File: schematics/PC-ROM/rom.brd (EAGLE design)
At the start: 40.1 x 49.6 mm, 23 parts

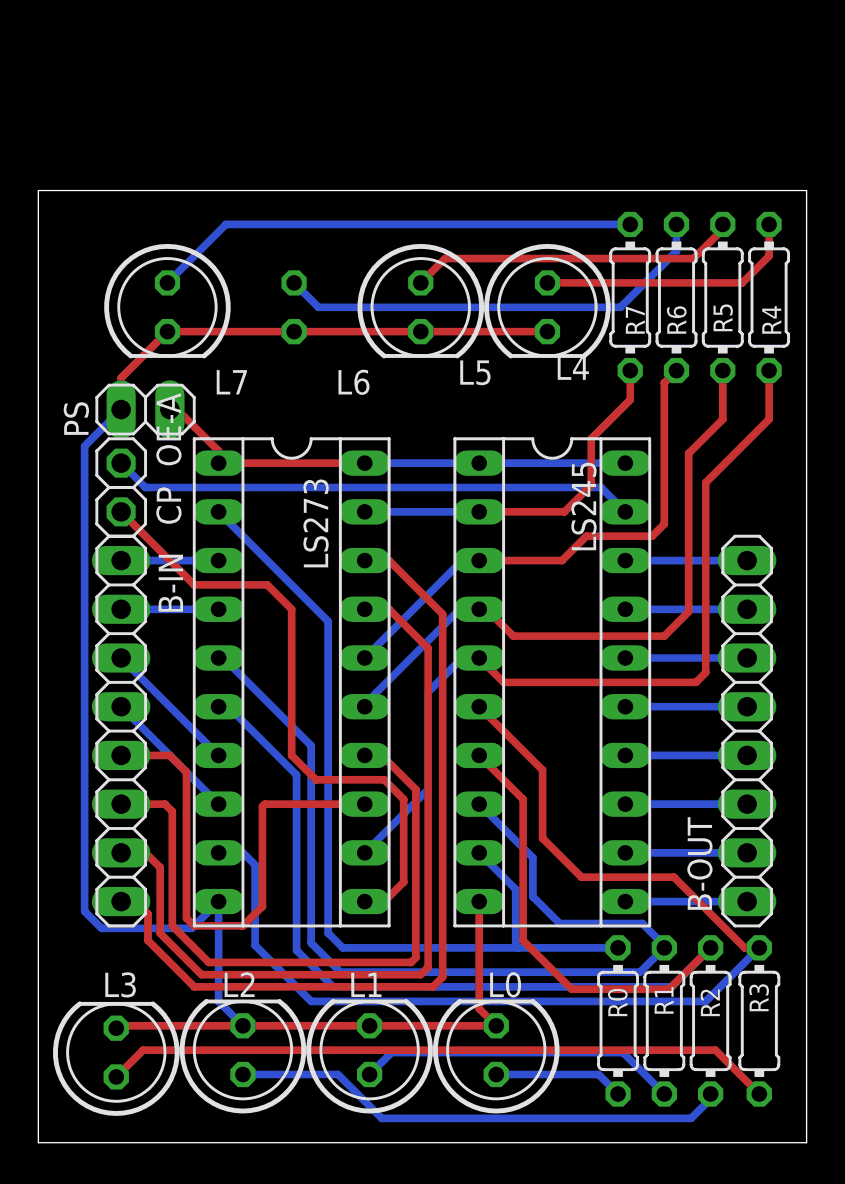
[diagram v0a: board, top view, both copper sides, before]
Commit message: Added sch, brd and gerber file for register, register bus, pc and ROM.
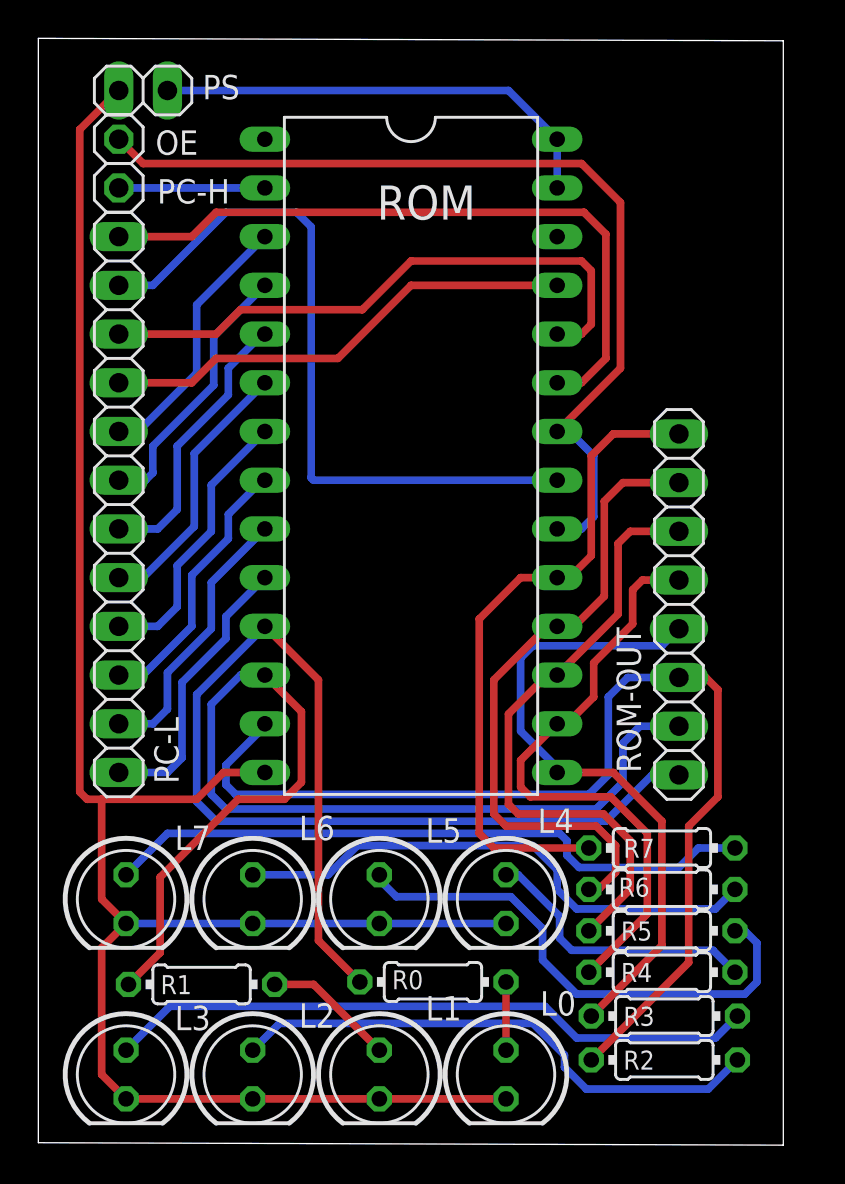
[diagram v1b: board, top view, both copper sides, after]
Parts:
- removed B-IN, B-OUT: (no value), pinhead:1X08
- removed CP, OE-A: (no value), pinhead:1X01
- removed LS245, LS273: (no value), ic-package:SOCKET-20
- added OE, PC-H: (no value), pinhead:1X01
- added PC-L: (no value), pinhead:1X12
- added ROM: (no value), ic-package:DIL28-6
- added ROM-OUT: (no value), pinhead:1X08
- moved R4 35.6 mm to (32.5, 8.89), turned to 180 degrees
- moved R5 33.2 mm to (32.5, 11.0), turned to 180 degrees
- moved L4 30.9 mm to (24.4, 12.7)
- moved L5 30.9 mm to (17.8, 12.7)
- moved L6 30.9 mm to (11.2, 12.7), flipped to the top
- moved L7 30.9 mm to (4.57, 12.7)
- moved R6 30.9 mm to (32.5, 13.2), turned to 180 degrees
- moved R7 28.7 mm to (32.5, 15.4), turned to 180 degrees
- moved R1 24.2 mm to (8.51, 8.26), turned to 180 degrees
- moved PS 16.6 mm to (5.46, 54.9)
- moved R0 9.86 mm to (20.6, 8.38), turned to 180 degrees
- moved R3 4.96 mm to (32.6, 6.60), turned to 180 degrees
- moved R2 3.15 mm to (32.6, 4.32), turned to 180 degrees
- moved L1 1.37 mm to (17.8, 3.56), turned to 270 degrees
- moved L2 1.37 mm to (11.2, 3.56), turned to 270 degrees
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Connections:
- removed net BO0: B-OUT.8, LS245.11
- removed net BO1: B-OUT.7, LS245.12
- removed net BO2: B-OUT.6, LS245.13
- removed net BO3: B-OUT.5, LS245.14
- removed net BO4: B-OUT.4, LS245.15
- removed net BO5: B-OUT.3, LS245.16
- removed net BO6: B-OUT.2, LS245.17
- removed net BO7: B-OUT.1, LS245.18
- removed net CP: CP.1, LS273.11
- removed net D0: B-IN.1, LS273.3
- removed net D1: B-IN.2, LS273.4
- removed net D2: B-IN.3, LS273.7
- removed net D3: B-IN.4, LS273.8
- removed net D4: B-IN.5, LS273.13
- removed net D5: B-IN.6, LS273.14
- removed net D6: B-IN.7, LS273.17
- removed net D7: B-IN.8, LS273.18
- removed net N$18: LS245.19, OE-A.1
- removed net Q0: LS245.9, LS273.2, R0.2
- removed net Q1: LS245.8, LS273.5, R1.2
- removed net Q2: LS245.7, LS273.6, R2.2
- removed net Q3: LS245.6, LS273.9, R3.2
- removed net Q4: LS245.5, LS273.12, R4.2
- removed net Q5: LS245.4, LS273.15, R5.2
- removed net Q6: LS245.3, LS273.16, R6.2
- removed net Q7: LS245.2, LS273.19, R7.2
- new net OE: OE.1, ROM.20, ROM.22
- new net PC0: PC-L.12, ROM.10
- new net PC1: PC-L.11, ROM.9
- new net PC10: PC-L.2, ROM.21
- new net PC11: PC-L.1, ROM.23
- new net PC12: PC-H.1, ROM.2
- new net PC2: PC-L.10, ROM.8
- new net PC3: PC-L.9, ROM.7
- new net PC4: PC-L.8, ROM.6
- new net PC5: PC-L.7, ROM.5
- new net PC6: PC-L.6, ROM.4
- new net PC7: PC-L.5, ROM.3
- new net PC8: PC-L.4, ROM.25
- new net PC9: PC-L.3, ROM.24
- new net ROM0: R0.2, ROM-OUT.8, ROM.11
- new net ROM1: R1.2, ROM-OUT.7, ROM.12
- new net ROM2: R2.2, ROM-OUT.6, ROM.13
- new net ROM3: R3.2, ROM-OUT.5, ROM.15
- new net ROM4: R4.2, ROM-OUT.4, ROM.16
- new net ROM5: R5.2, ROM-OUT.3, ROM.17
- new net ROM6: R6.2, ROM-OUT.2, ROM.18
- new net ROM7: R7.2, ROM-OUT.1, ROM.19
- net GND: now also ROM.14; no longer LS245.10, LS273.10
- net VCC: now also ROM.27, ROM.28; no longer LS245.1, LS245.20, LS273.1, LS273.20
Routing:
- net Q2: track 60.2 -> 0.00 mm
- net ROM1: track 0.00 -> 57.9 mm
- net ROM0: track 0.00 -> 57.8 mm
- net ROM2: track 0.00 -> 57.1 mm
- net Q3: track 56.9 -> 0.00 mm
- net Q1: track 50.6 -> 0.00 mm
- net OE: track 0.00 -> 48.6 mm
- net Q0: track 45.6 -> 0.00 mm
- net D7: track 43.8 -> 0.00 mm
- net Q4: track 42.8 -> 0.00 mm
- net D6: track 41.6 -> 0.00 mm
- net PC10: track 0.00 -> 37.9 mm
- net PC11: track 0.00 -> 35.9 mm
- net ROM7: track 0.00 -> 34.7 mm
- net D5: track 34.6 -> 0.00 mm
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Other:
- board size 40.1 x 49.6 mm -> 38.8 x 57.7 mm
